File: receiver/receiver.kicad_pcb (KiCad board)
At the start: 2 copper layers, 50 x 50 mm, 22 parts, among them CON1 AVR-ISP-6, IC1 ATTINY441-SSU, P1 CONN_02X07, P2 CONN_01X01, P3 CONN_01X02, U1 LD1117S12CTR, U2 LM393, U3 MC4018

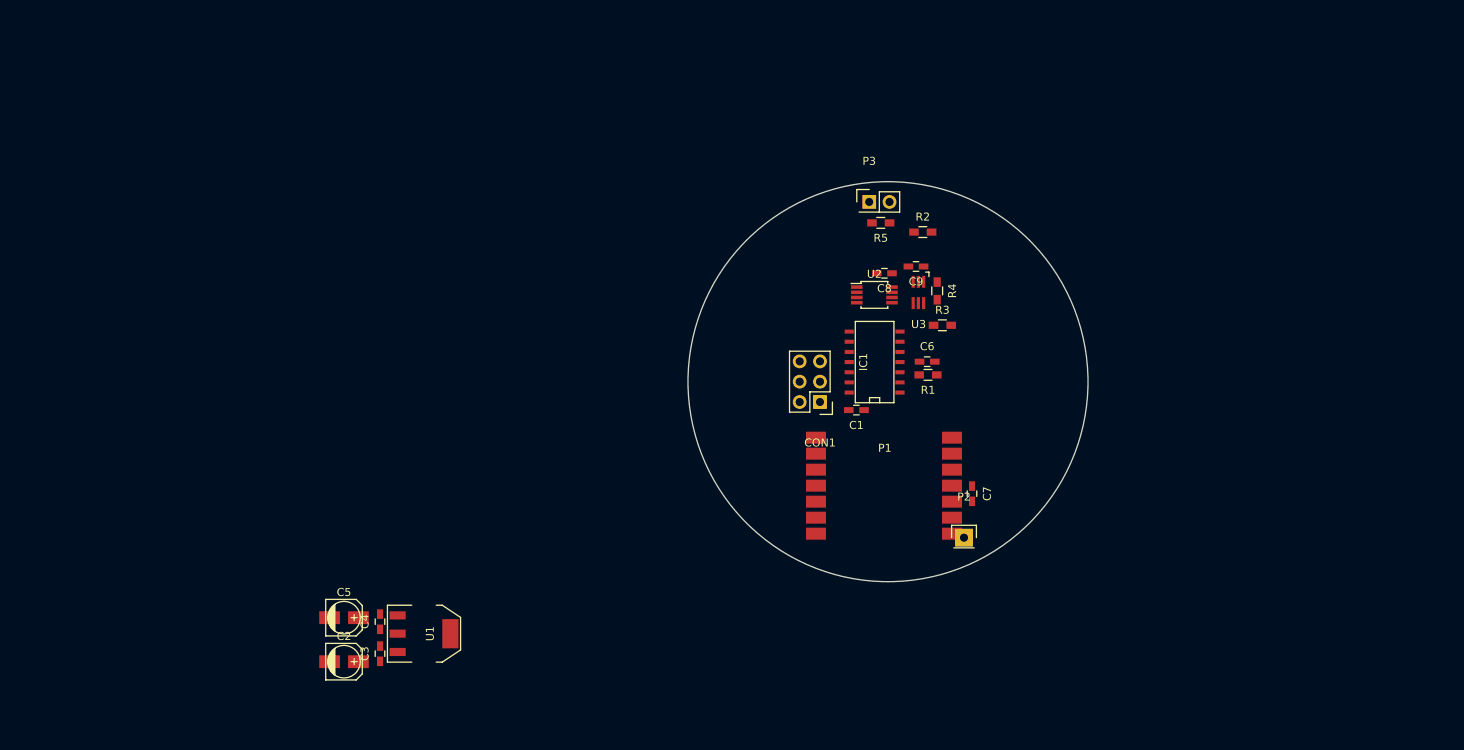
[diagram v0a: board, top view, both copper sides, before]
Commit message: Schematics changes: change RF module to RFM69, add onboard phototransistors, add a switch for laser, put programming header on proper pins, add PTC to the power supply, add voltage measurement divider and led
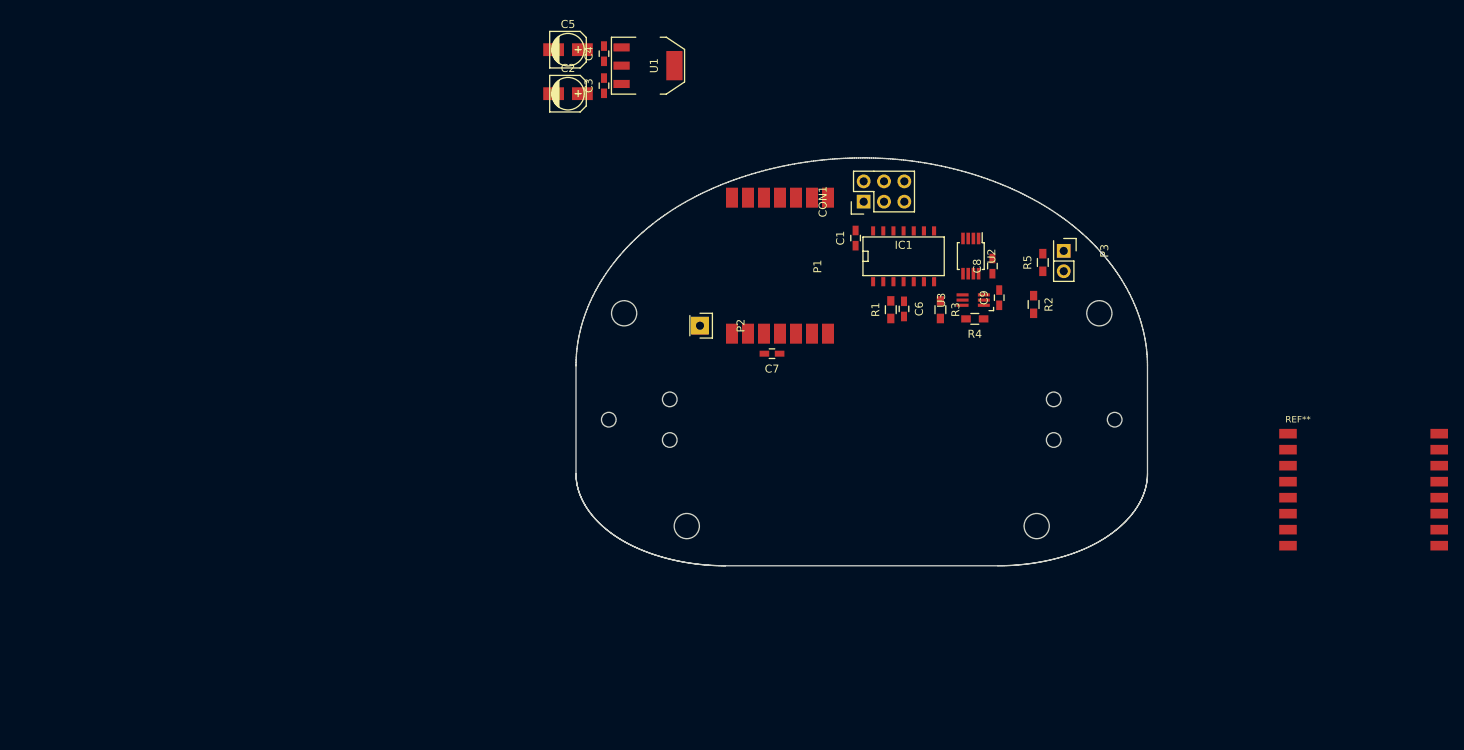
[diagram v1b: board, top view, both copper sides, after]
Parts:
- added REF**: RFM69HW, mysensors_radios:RFM69HW_SMD, F.Cu at (211.0, 96.5)
- moved C2 76.3 mm to (120.0, 54.0)
- moved C3 76.3 mm to (124.5, 53.0)
- moved C4 76.3 mm to (124.5, 49.0)
- moved C5 76.3 mm to (120.0, 48.5)
- moved U1 76.3 mm to (130.0, 50.5)
- moved P2 42.3 mm to (136.5, 83.0), turned to 270 degrees
- moved C7 30.5 mm to (145.5, 86.5), turned to 180 degrees
- moved P1 30.4 mm to (146.5, 75.5), turned to 270 degrees
- moved CON1 25.6 mm to (157.0, 67.5), turned to 90 degrees
- moved P3 25.1 mm to (182.0, 73.7), turned to 270 degrees
- moved C1 21.5 mm to (155.9, 72.0), turned to 90 degrees
- moved R5 20.8 mm to (179.3, 75.1), turned to 90 degrees
- moved R2 16.5 mm to (178.2, 80.3), turned to 270 degrees
- moved IC1 13.9 mm to (161.9, 74.2), turned to 0 degrees
- moved C8 13.5 mm to (173.1, 75.5), turned to 90 degrees
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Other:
- board size 50 x 50 mm -> 71.4 x 51 mm

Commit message: New PCB outline. Add 3D models to PCB. Start routing
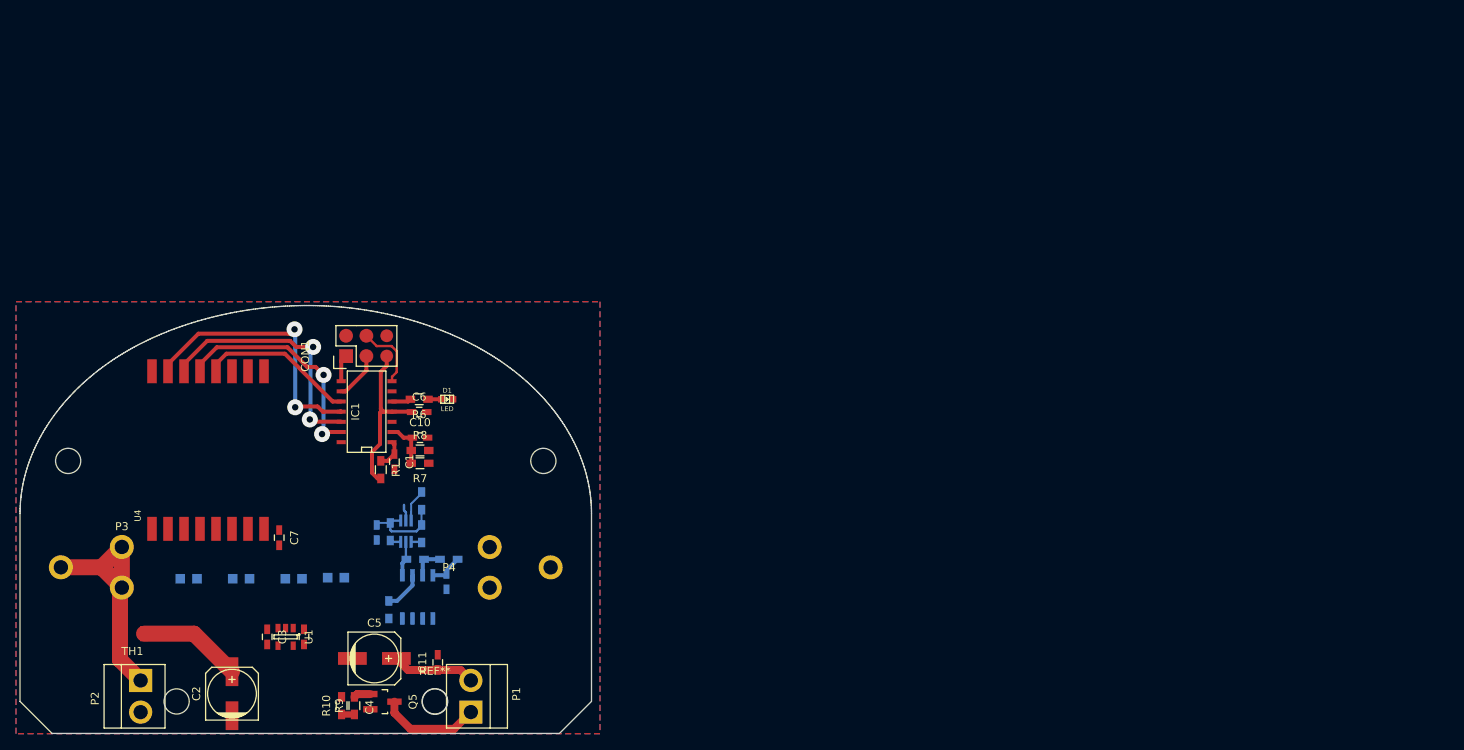
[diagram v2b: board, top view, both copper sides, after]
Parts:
- removed the REF** at (211.0, 96.5)
- added C10: 1u, Capacitors_SMD:C_0603_HandSoldering, F.Cu at (101.5, 97.0)
- added C11: 1u, Capacitors_SMD:C_0603_HandSoldering, F.Cu at (103.7, 125.1)
- added D1: LED, w_smd_leds:Led_0603, F.Cu at (104.9, 92.2)
- added P4: CONN_01X01, Pin_Headers:Pin_Header_Straight_1x01, F.Cu at (110.2, 113.2)
- added Q1: OPTO_NPN, w_smd_leds:Led_0805, B.Cu at (72.6, 114.6)
- added Q2: OPTO_NPN, w_smd_leds:Led_0805, B.Cu at (91.0, 114.5)
- added Q3: OPTO_NPN, w_smd_leds:Led_0805, B.Cu at (79.1, 114.6)
- added Q4: OPTO_NPN, w_smd_leds:Led_0805, B.Cu at (85.7, 114.6)
- added Q5: Q_NMOS_GDS, Housings_SOT-23_SOT-143_TSOT-6:SOT-23_Handsoldering, F.Cu at (96.8, 130.0)
- added R10: 512k, Resistors_SMD:R_0603_HandSoldering, F.Cu at (91.7, 130.5)
- added R11: 4.7k, Resistors_SMD:R_0603_HandSoldering, B.Cu at (101.7, 109.0)
- added R12: 4.7k, Resistors_SMD:R_0603_HandSoldering, B.Cu at (101.7, 104.9)
- added R6: 220, Resistors_SMD:R_0603_HandSoldering, F.Cu at (101.4, 92.2)
- added R7: 10k, Resistors_SMD:R_0603_HandSoldering, F.Cu at (101.5, 100.2)
- added R8: 10k, Resistors_SMD:R_0603_HandSoldering, F.Cu at (101.5, 98.6)
- added R9: 220, Resistors_SMD:R_0603_HandSoldering, F.Cu at (93.3, 130.5)
- added REF**: MountingHole_3.2mm_M3_DIN965, Mounting_Holes:MountingHole_3.2mm_M3_DIN965, F.Cu at (103.4, 130.0)
- added TH1: MC33191, Fuse_Holders_and_Fuses:Fuse_SMD1206_HandSoldering, F.Cu at (65.5, 121.5)
- added U4: RFM69HW, mysensors_radios:RFM69HW_SMD_Handsoldering, F.Cu at (68.0, 107.0)
- C2, C5: footprint Capacitors_SMD:c_elec_4x4.5 -> Capacitors_SMD:c_elec_6.3x5.3
- C8, C9, R2, R3, R4, R5, U3: moved to B.Cu
- P1: value CONN_02X07 -> LASER; footprint Pin_Headers:Pin_Header_Angled_2x07 -> Pin_Headers:Pin_Header_Straight_1x02_Pitch3.96mm_Friction_Lock
- P2: value CONN_01X01 -> BATTERY; footprint Pin_Headers:Pin_Header_Straight_1x01 -> Pin_Headers:Pin_Header_Straight_1x02_Pitch3.96mm_Friction_Lock
- P3: value CONN_01X02 -> CONN_01X01; footprint Pin_Headers:Pin_Header_Straight_2x01 -> Pin_Headers:Pin_Header_Straight_1x01
- U1: value LD1117S12CTR -> MIC5504-3.3; footprint SMD_Packages:SOT-223 -> Housings_SOT-23_SOT-143_TSOT-6:SOT-23-5
- U2: footprint Housings_SSOP:MSOP-8_3x3mm_Pitch0.65mm -> Housings_SOIC:SOIC-8_3.9x4.9mm_Pitch1.27mm; moved to B.Cu
- moved P3 124.2 mm to (64.2, 113.2), turned to 0 degrees
- moved R5 92.6 mm to (97.6, 118.5), turned to 270 degrees
- moved C2 86.0 mm to (78.0, 129.0), turned to 90 degrees
- moved U1 84.6 mm to (84.7, 121.9)
- moved C9 83.2 mm to (96.1, 108.9), turned to 270 degrees
- moved P2 82.8 mm to (66.6, 127.3)
- moved C4 82.0 mm to (87.0, 121.9), turned to 270 degrees
- moved U2 81.2 mm to (101.2, 116.9), turned to 90 degrees
- moved C3 80.7 mm to (82.4, 121.9), turned to 270 degrees
- moved C5 79.9 mm to (95.8, 124.6)
- moved R2 79.7 mm to (105.1, 112.2), turned to 180 degrees
- moved C8 78.8 mm to (104.8, 115.0), turned to 270 degrees
- moved R4 77.8 mm to (97.8, 108.8), turned to 270 degrees
- moved U3 76.6 mm to (99.7, 108.7), turned to 0 degrees
- moved R3 72.7 mm to (100.9, 112.2), turned to 0 degrees
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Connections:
- net Net-(C6-Pad1) renamed /RESET
- net Net-(IC1-Pad3) renamed /LASER_DETECT
- net Net-(R3-Pad1) renamed /THRESHOLD
- C5 pad 1: VCC -> VAA
- CON1 pad 1: Net-(CON1-Pad1) -> /LASER_ON/MISO
- CON1 pad 2: VCC -> (no net)
- CON1 pad 3: /SCK -> /SCK/SCL
- CON1 pad 4: /SDI -> /SDA
- IC1 pad 10: /SCK -> /RADIO_SCK
- IC1 pad 11: /NSEL -> /RADIO_SELECT
- IC1 pad 12: /SDI -> /RADIO_MOSI
- IC1 pad 13: Net-(CON1-Pad1) -> /RADIO_MISO
- IC1 pad 2: Net-(IC1-Pad2) -> /BATTERY_VOLTAGE
- IC1 pad 5: Net-(IC1-Pad5) -> /LED
- IC1 pad 6: Net-(IC1-Pad6) -> /INT
- IC1 pad 7: Net-(IC1-Pad7) -> /SDA
- IC1 pad 8: /NIRQ -> /LASER_ON/MISO
- IC1 pad 9: Net-(IC1-Pad9) -> /SCK/SCL
- P1 pad 1: /SDI -> Net-(P1-Pad1)
- P1 pad 2: /NIRQ -> VAA
- P2 pad 1: /ANT -> +BATT
- P3 pad 1: VCC -> +BATT
- R5 pad 1: Net-(P3-Pad2) -> /MATRIX_OUT
- U2 pad 6: Net-(P3-Pad2) -> /MATRIX_OUT
- U3 pad 3: Net-(IC1-Pad9) -> /SCK/SCL
- U3 pad 4: Net-(IC1-Pad7) -> /SDA
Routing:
- net /RADIO_SELECT: track 0.00 -> 34.7 mm, vias 0 -> 2
- net /RADIO_MOSI: track 0.00 -> 31.9 mm, vias 0 -> 2
- net +BATT: track 0.00 -> 30.1 mm
- net /RADIO_MISO: track 0.00 -> 28.6 mm, vias 0 -> 2
- net VAA: track 0.00 -> 23.6 mm
- net /RESET: track 0.00 -> 20.8 mm
- net /RADIO_SCK: track 0.00 -> 19.6 mm
- net VCC: track 0.00 -> 18.3 mm
- net Net-(P1-Pad1): track 0.00 -> 12.7 mm
- net /SCK/SCL: track 0.00 -> 10.5 mm
- net /SDA: track 0.00 -> 9.92 mm
- net /BATTERY_VOLTAGE: track 0.00 -> 6.10 mm
- net /LASER_ON/MISO: track 0.00 -> 5.99 mm
- net /MATRIX_OUT: track 0.00 -> 5.04 mm
- net /THRESHOLD: track 0.00 -> 4.41 mm
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- added copper zone on B.Cu, net GND
- added copper zone on F.Cu, net GND
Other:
- board size 71.4 x 51 mm -> 71.4 x 53.5 mm
- net class Default: trace_width 0.25 -> 0.3; via_dia 0.6 -> 2; via_drill 0.4 -> 0.8
